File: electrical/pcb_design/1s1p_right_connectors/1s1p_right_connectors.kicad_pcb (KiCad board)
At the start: 4 copper layers, 77 x 96 mm, 37 parts, among them J10 TE_Connectivity_7-5530843-7, J11 TE_Connectivity_7-5530843-7, J12 TE_Connectivity_7-5530843-7, J13 TE_Connectivity_7-5530843-7, J14 TE_Connectivity_7-5530843-7, J15 TE_Connectivity_7-5530843-7, J16 TE_Connectivity_7-5530843-7, J17 STLINK_TagConnect_6, J9 TE_Connectivity_7-5530843-7, U1 BMI323, U2 BMI323, U3 TCAN330, U4 STM32L452CEU6

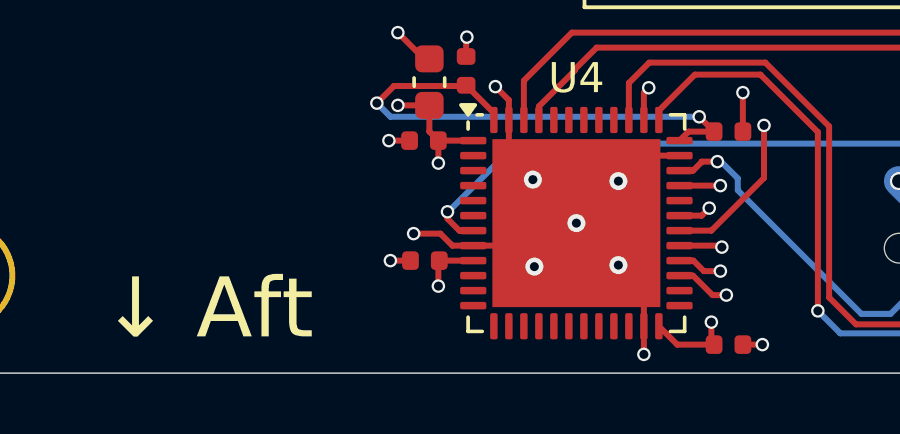
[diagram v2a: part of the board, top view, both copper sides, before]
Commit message: Added board identification mechanism. Updated production files and 3D models.
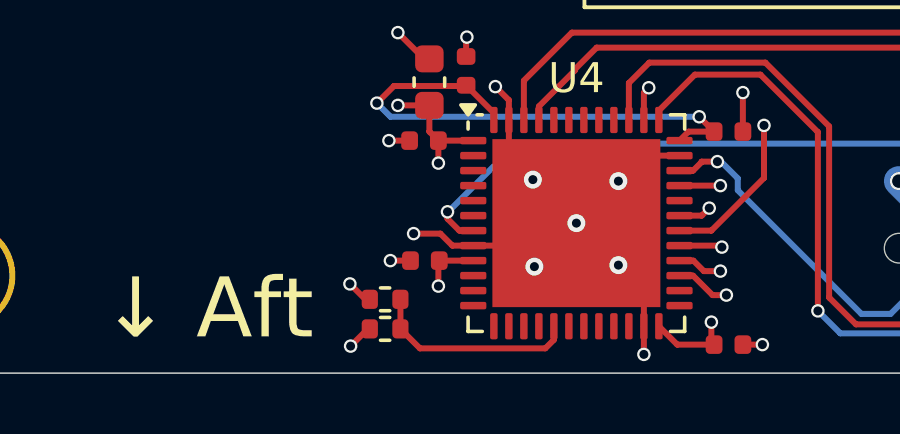
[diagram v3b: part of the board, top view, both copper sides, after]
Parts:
- added R4: 845k, footprints:Nondescript_R_0402_1005Metric, F.Cu at (146.5, 131.9)
- added R5: 120k, footprints:Nondescript_R_0402_1005Metric, F.Cu at (146.5, 130.9)
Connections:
- U4 pad 17: unconnected-(U4-PA7-Pad17) -> BOARD_ID
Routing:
- net BOARD_ID: track 0.00 -> 6.94 mm
- net +3.3V: track 39.2 -> 40.1 mm, vias 17 -> 18
- net GND: track 131.8 -> 132.7 mm, vias 23 -> 24

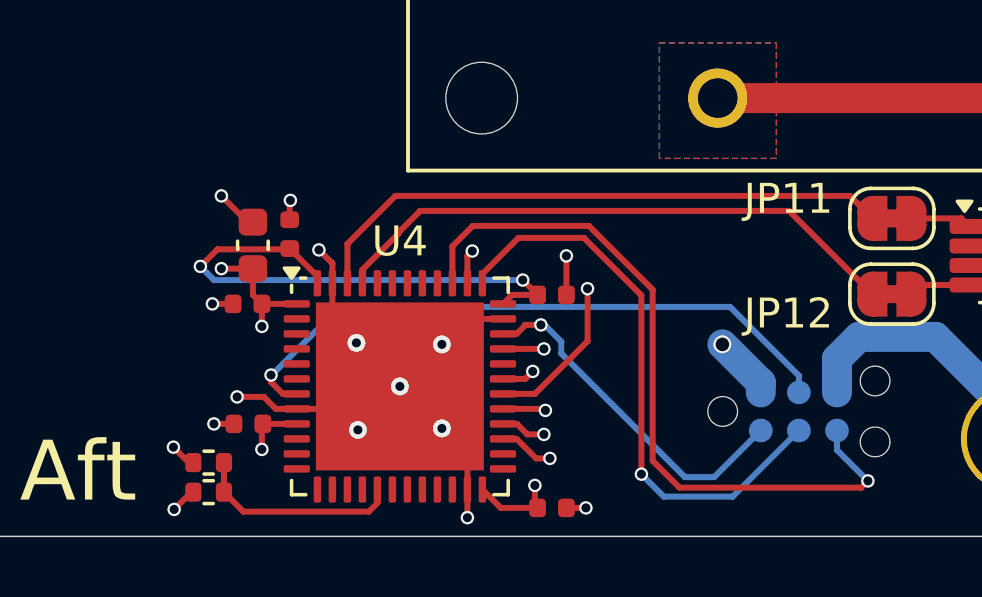
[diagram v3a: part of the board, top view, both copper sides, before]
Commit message: Modified PCB designs to use local footprint for the STM32L452CEU6 part in order to configure the 3D model for this part.
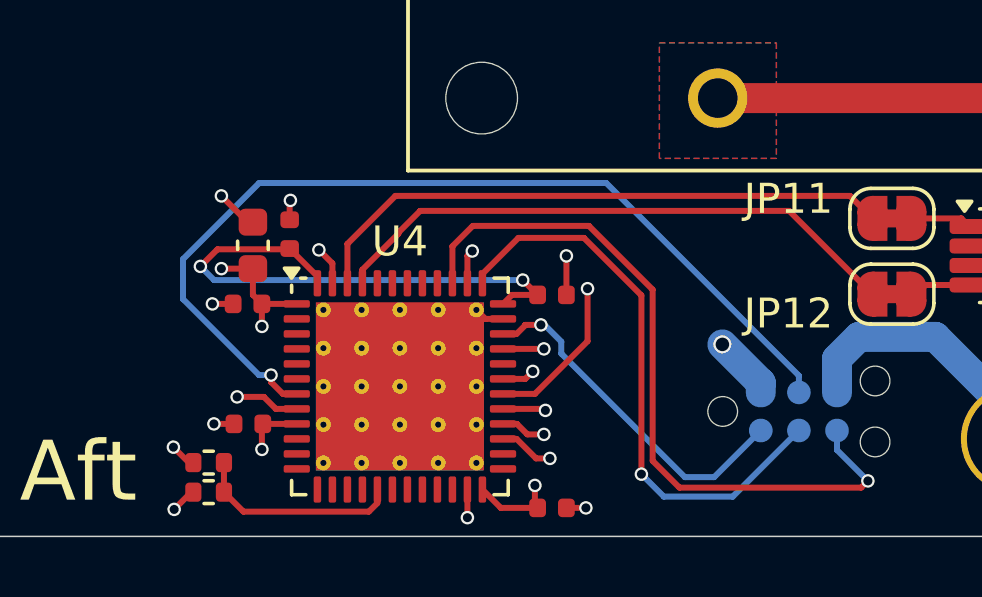
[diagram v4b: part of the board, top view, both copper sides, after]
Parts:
- U4: footprint Package_DFN_QFN:QFN-48-1EP_7x7mm_P0.5mm_EP5.6x5.6mm -> footprints:QFN-48-1EP_7x7mm_P0.5mm_EP5.6x5.6mm_ThermalVias
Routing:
- net NRST: track 21.3 -> 31.4 mm
- net GND: track 132.7 -> 128.6 mm, vias 24 -> 19
- net IMU1_INT1: track 69.8 -> 70.5 mm

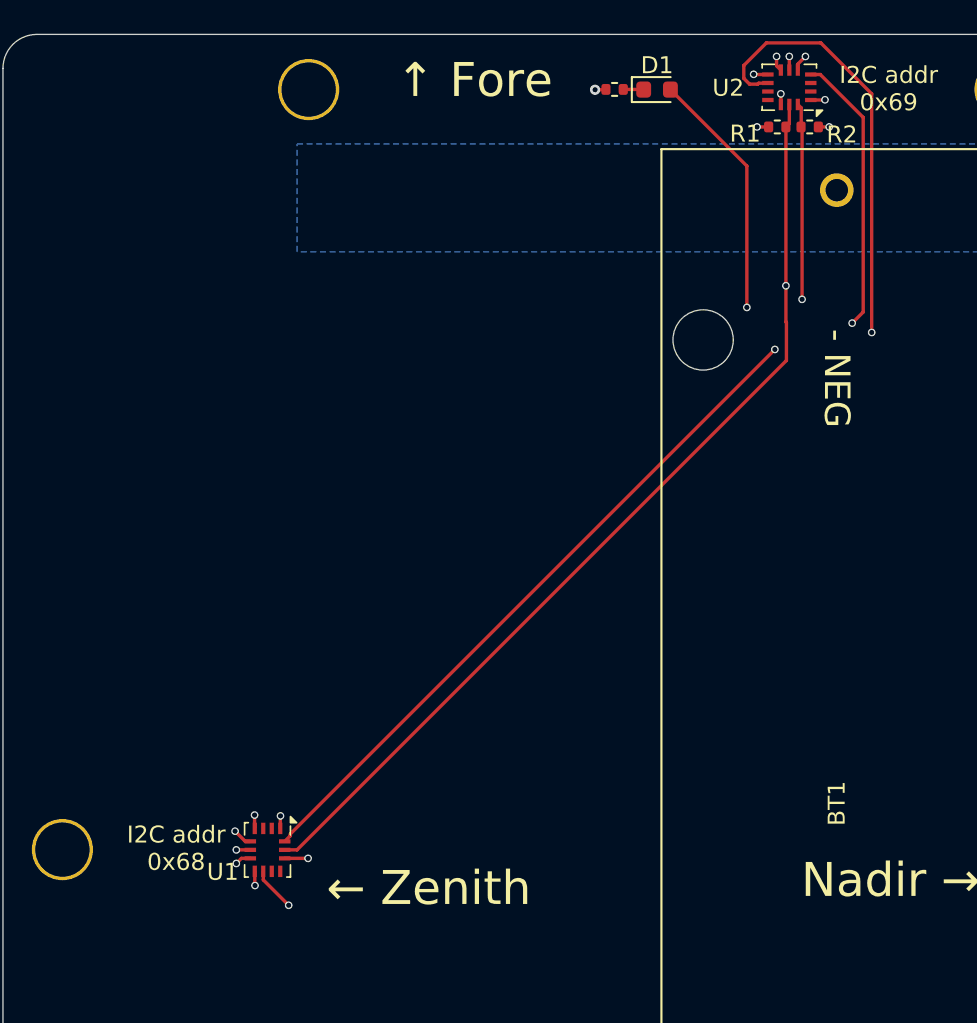
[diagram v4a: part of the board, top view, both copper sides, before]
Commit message: Added decoupling capacitors for IMUs on battery boards
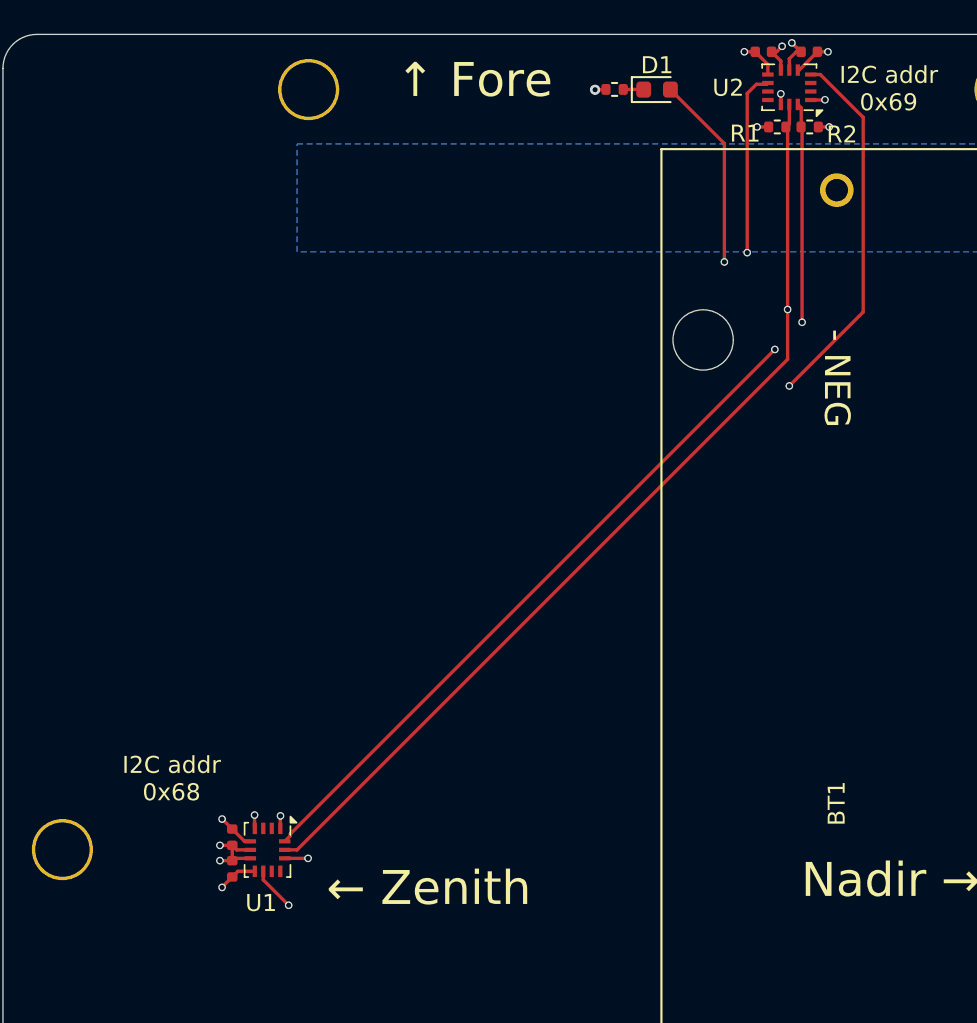
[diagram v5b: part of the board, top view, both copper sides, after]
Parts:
- added C11: 100n, footprints:Nondescript_C_0402_1005Metric, F.Cu at (161.9, 38.4)
- added C12: 100n, footprints:Nondescript_C_0402_1005Metric, F.Cu at (159.2, 38.4)
- added C7: 100n, footprints:Nondescript_C_0402_1005Metric, F.Cu at (127.9, 84.6)
- added C8: 100n, footprints:Nondescript_C_0402_1005Metric, F.Cu at (127.9, 86.5)
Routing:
- net IMU2_INT2: track 106.6 -> 96.5 mm
- net GND: track 128.6 -> 134.1 mm
- net +3.3V: track 40.1 -> 45.3 mm
- net I2C1_SCL: track 135.4 -> 134.1 mm

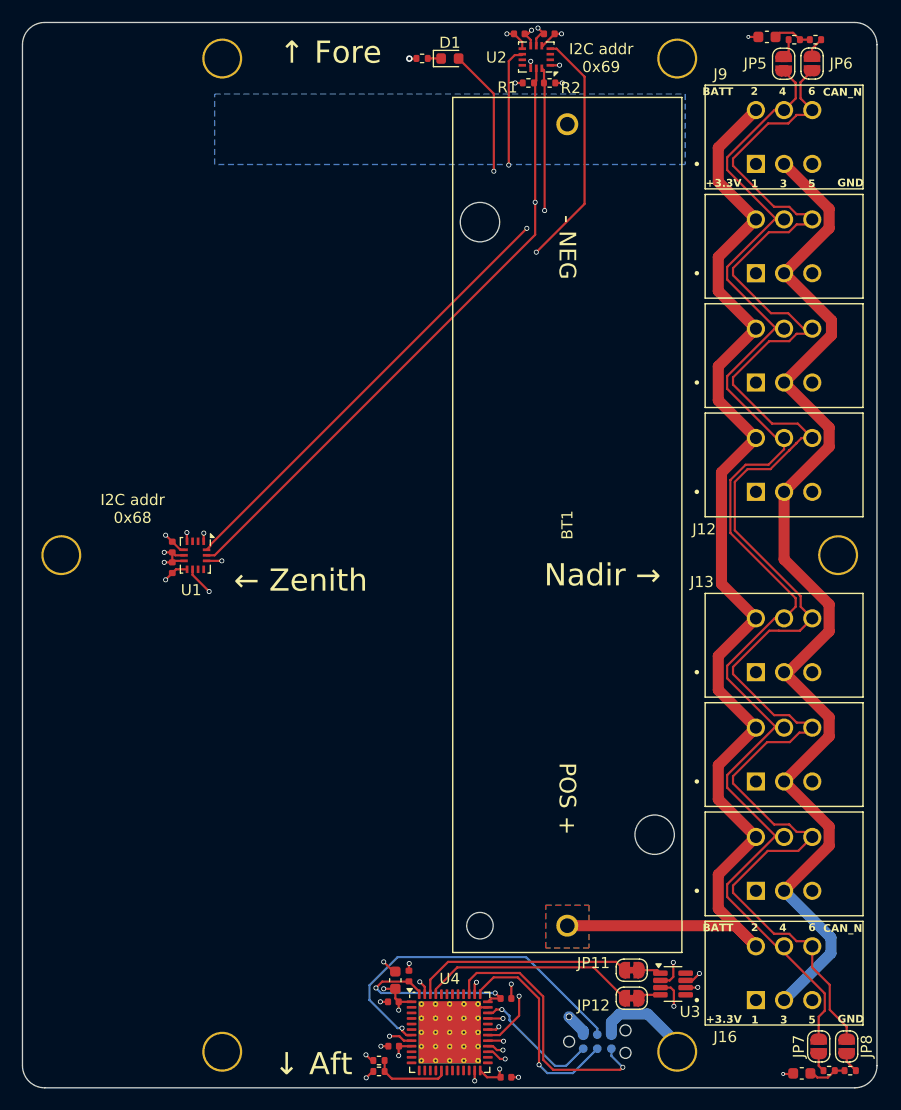
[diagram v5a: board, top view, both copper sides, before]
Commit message: Incorporated feedback on schematic and pcb for one board. Next step will be to translate this to the other boards.
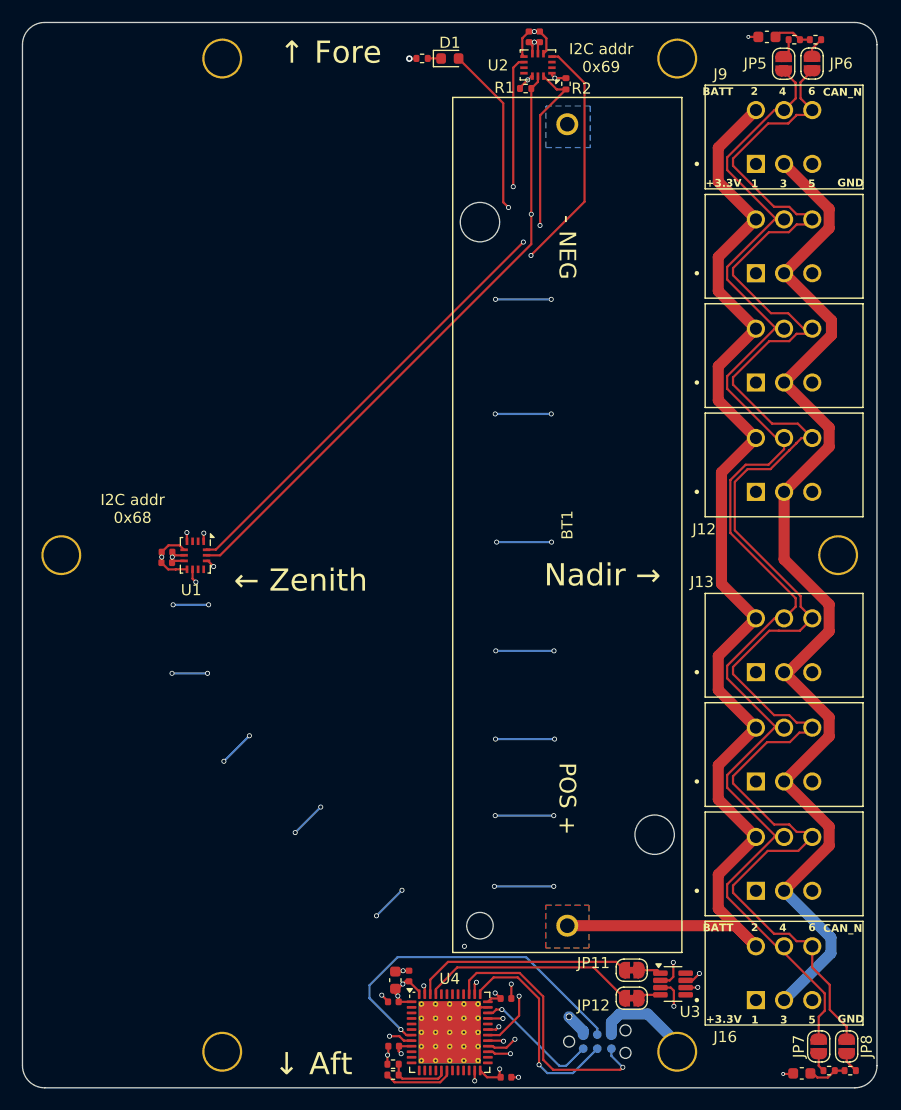
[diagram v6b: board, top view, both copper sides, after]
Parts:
- C2: value 100n -> 10n
- moved R5 1.82 mm to (147.8, 132.2)
- moved R2 1.48 mm to (163.4, 42.9), turned to -90 degrees
- moved R4 1.43 mm to (147.8, 131.2)
- moved C11 0.92 mm to (161.0, 38.6), turned to -90 degrees
- moved C12 0.92 mm to (160.1, 38.6), turned to -90 degrees
- moved U2 0.73 mm to (160.9, 41.2)
- moved C8 0.68 mm to (127.4, 86.0), turned to 0 degrees
- moved C7 0.66 mm to (127.4, 85.1), turned to 0 degrees
- moved R1 0.56 mm to (159.8, 43.3)
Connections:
- net BOARD_ID renamed /MCU/BOARD_ID
- net IMU1_INT1 renamed /MCU/IMU1_INT1
- net IMU1_INT2 renamed /MCU/IMU1_INT2
- net IMU2_INT1 renamed /MCU/IMU2_INT1
- net IMU2_INT2 renamed /MCU/IMU2_INT2
- net NRST renamed /MCU/NRST
- net SWCLK renamed /MCU/SWCLK
- net SWDIO renamed /MCU/SWDIO
- net TRACESWO renamed /MCU/TRACESWO
- R5 pad 1: +3.3V -> /MCU/BOARD_ID_CTRL
- U4 pad 18: unconnected-(U4-PB0-Pad18) -> /MCU/BOARD_ID_CTRL
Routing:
- net +3.3V: track 45.3 -> 90.5 mm, vias 18 -> 37
- net /MCU/IMU1_INT1: track 70.5 -> 61.0 mm
- net /MCU/BOARD_ID_CTRL: track 0.00 -> 6.35 mm
- net GND: track 134.1 -> 130.9 mm, vias 19 -> 15
- net /MCU/IMU2_INT2: track 96.5 -> 94.8 mm
- net /MCU/BOARD_ID: track 6.94 -> 5.54 mm
- net I2C1_SCL: track 134.1 -> 132.8 mm
- net /MCU/IMU2_INT1: track 96.5 -> 95.5 mm
- net I2C1_SDA: track 130.8 -> 131.5 mm
